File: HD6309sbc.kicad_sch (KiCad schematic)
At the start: 24 parts, among them J1 Conn_01x02_Male, J3 Conn_01x02_Male, U1 HD63C09, U11 74HC02, U12 74AHC1G08, U13 74HC21D, U14 74HC21D, U15 74HC21D, U4 UM61256FK, U6 28C256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

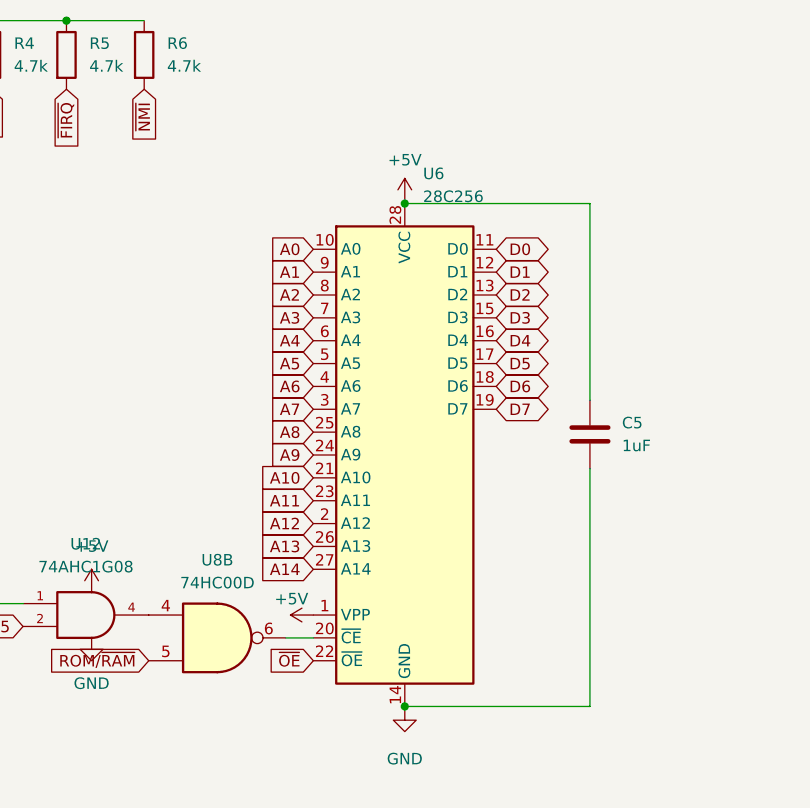
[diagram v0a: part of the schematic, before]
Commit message: fix rom footprint
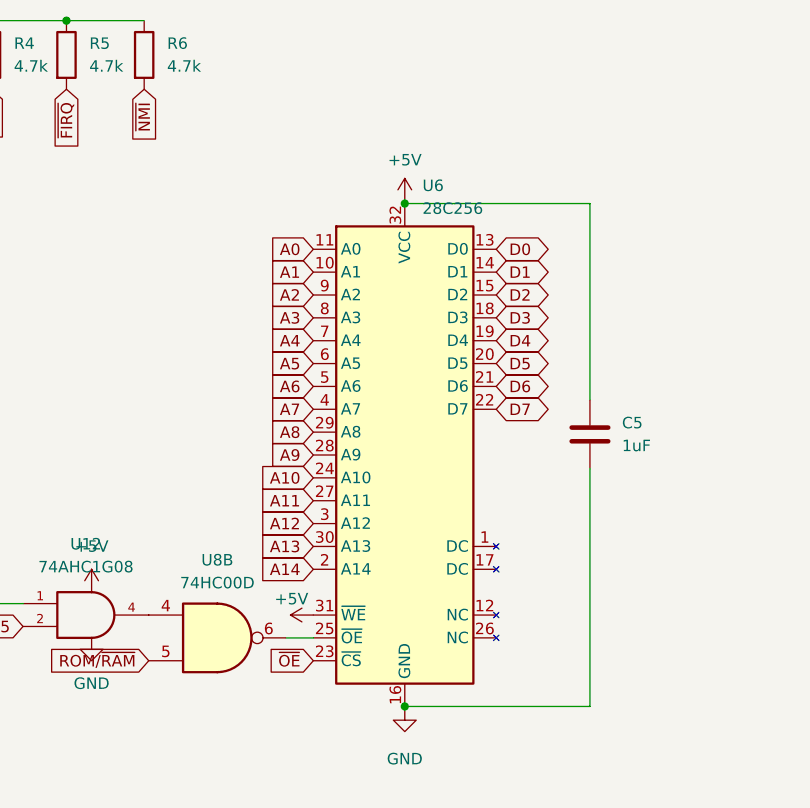
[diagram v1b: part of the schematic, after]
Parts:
- removed U6: 28C256, Package_LCC:PLCC-28_THT-Socket, symbol Memory_EPROM:27C256
- added U6: 28C256, Package_LCC:PLCC-32_THT-Socket, symbol 6309sbc:28C256plcc
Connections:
- net +5V: now also U6.31 (~{WE}), U6.32 (VCC)
- net A0: now also U6.11 (A0)
- net A1: now also U6.10 (A1)
- net A10: now also U6.24 (A10)
- net A11: now also U6.27 (A11)
- net A12: now also U6.3 (A12)
- net A13: now also U6.30 (A13)
- net A14: now also U6.2 (A14)
- net A2: now also U6.9 (A2)
- net A3: now also U6.8 (A3)
- net A4: now also U6.7 (A4)
- net A5: now also U6.6 (A5)
- net A6: now also U6.5 (A6)
- net A7: now also U6.4 (A7)
- net A8: now also U6.29 (A8)
- net A9: now also U6.28 (A9)
- net D0: now also U6.13 (D0)
- net D1: now also U6.14 (D1)
- net D2: now also U6.15 (D2)
- net D3: now also U6.18 (D3)
- net D4: now also U6.19 (D4)
- net D5: now also U6.20 (D5)
- net D6: now also U6.21 (D6)
- net D7: now also U6.22 (D7)
- net GND: now also U6.16 (GND)
- net ~{OE}: now also U6.23 (~{CS})
- net at U8.6: now also U6.25 (~{OE})
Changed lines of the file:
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@@
   (junction (at 35.306 25.654) (diameter 0) (color 0 0 0 0)
   )
+  (junction (at 42.926 25.654) (diameter 0) (color 0 0 0 0)
+  )
+  (junction (at 36.576 30.48) (diameter 0) (color 0 0 0 0)
+  )
+  (junction (at 38.1 191.262) (diameter 0) (color 0 0 0 0)
+  )
   (junction (at 147.574 132.08) (diameter 0) (color 0 0 0 0)
   )
-  (junction (at 42.926 25.654) (diameter 0) (color 0 0 0 0)
-  )
-  (junction (at 36.576 30.48) (diameter 0) (color 0 0 0 0)
-  )
-  (junction (at 38.1 191.262) (diameter 0) (color 0 0 0 0)
+  (junction (at 154.686 29.972) (diameter 0) (color 0 0 0 0)
+  )
+  (junction (at 93.218 111.76) (diameter 0) (color 0 0 0 0)
+  )
+  (junction (at 38.1 146.812) (diameter 0) (color 0 0 0 0)
   )
   (junction (at 147.574 187.96) (diameter 0) (color 0 0 0 0)
-  )
-  (junction (at 154.686 29.972) (diameter 0) (color 0 0 0 0)
-  )
-  (junction (at 93.218 111.76) (diameter 0) (color 0 0 0 0)
-  )
-  (junction (at 38.1 146.812) (diameter 0) (color 0 0 0 0)
   )
   (junction (at 101.6 111.76) (diameter 0) (color 0 0 0 0)
@@
         (path "/b6976bcd-dc73-4942-aa19-f7adbf9104c7"
           (reference "#PWR018") (unit 1)
+        )
+      )
+    )
+  )
+  (symbol (lib_id "6309sbc:28C256plcc") (at 147.574 160.02 0) (unit 1)
+    (in_bom yes) (on_board yes) (dnp no) (fields_autoplaced)
+    (property "Reference" "U6" (at 149.5299 130.0988 0)
+      (effects (font (size 1.27 1.27)) (justify left))
+    )
+    (property "Value" "28C256" (at 149.5299 132.6388 0)
+      (effects (font (size 1.27 1.27)) (justify left))
+    )
+    (property "Footprint" "Package_LCC:PLCC-32_THT-Socket" (at 147.574 160.02 0)
+      (effects (font (size 1.27 1.27)) hide)
+    )
+    (property "Datasheet" "http://ww1.microchip.com/downloads/en/DeviceDoc/doc0006.pdf" (at 147.574 160.02 0)
+      (effects (font (size 1.27 1.27)) hide)
+    )
+    (pin "1")
+    (pin "10")
+    (pin "11")
+    (pin "12")
+    (pin "13")
+    (pin "14")
+    (pin "15")
+    (pin "16")
+    (pin "17")
+    (pin "18")
+    (pin "19")
+    (pin "2")
+    (pin "20")
+    (pin "21")
+    (pin "22")
+    (pin "23")
+    (pin "24")
+    (pin "25")
+    (pin "26")
+    (pin "27")
+    (pin "28")
+    (pin "29")
+    (pin "3")
+    (pin "30")
+    (pin "31")
+    (pin "32")
+    (pin "4")
+    (pin "5")
+    (pin "6")
+    (pin "7")
+    (pin "8")
+    (pin "9")
+    (instances
+      (project "HD6309sbc"
+        (path "/b6976bcd-dc73-4942-aa19-f7adbf9104c7"
+          (reference "U6") (unit 1)
         )
       )
@@
         )
       )
-    )
-  )
-  (symbol (lib_id "Memory_EPROM:27C256") (at 147.574 160.02 0) (unit 1)
-    (in_bom yes) (on_board yes) (dnp no) (fields_autoplaced)
-    (property "Reference" "U6" (at 149.5934 128.778 0)
-      (effects (font (size 1.27 1.27)) (justify left))
-    )
-    (property "Value" "28C256" (at 149.5934 131.318 0)
-      (effects (font (size 1.27 1.27)) (justify left))
-    )
-    (property "Footprint" "Package_LCC:PLCC-28_THT-Socket" (at 147.574 160.02 0)
-      (effects (font (size 1.27 1.27)) hide)
-    )
-    (property "Datasheet" "http://ww1.microchip.com/downloads/en/DeviceDoc/doc0014.pdf" (at 147.574 160.02 0)
-      (effects (font (size 1.27 1.27)) hide)
-    )
-    (property "Note" "High 32k ROM" (at 147.574 160.02 0)
-      (effects (font (size 1.27 1.27)) hide)
-    )
-    (pin "1")
-    (pin "10")
-    (pin "11")
-    (pin "12")
-    (pin "13")
-    (pin "14")
-    (pin "15")
-    (pin "16")
-    (pin "17")
-    (pin "18")
-    (pin "19")
-    (pin "2")
-    (pin "20")
-    (pin "21")
-    (pin "22")
-    (pin "23")
-    (pin "24")
-    (pin "25")
-    (pin "26")
-    (pin "27")
-    (pin "28")
-    (pin "3")
-    (pin "4")
-    (pin "5")
-    (pin "6")
-    (pin "7")
-    (pin "8")
-    (pin "9")
-    (instances
-      (project "HD6309sbc"
-        (path "/b6976bcd-dc73-4942-aa19-f7adbf9104c7"
-          (reference "U6") (unit 1)
-        )
-      )

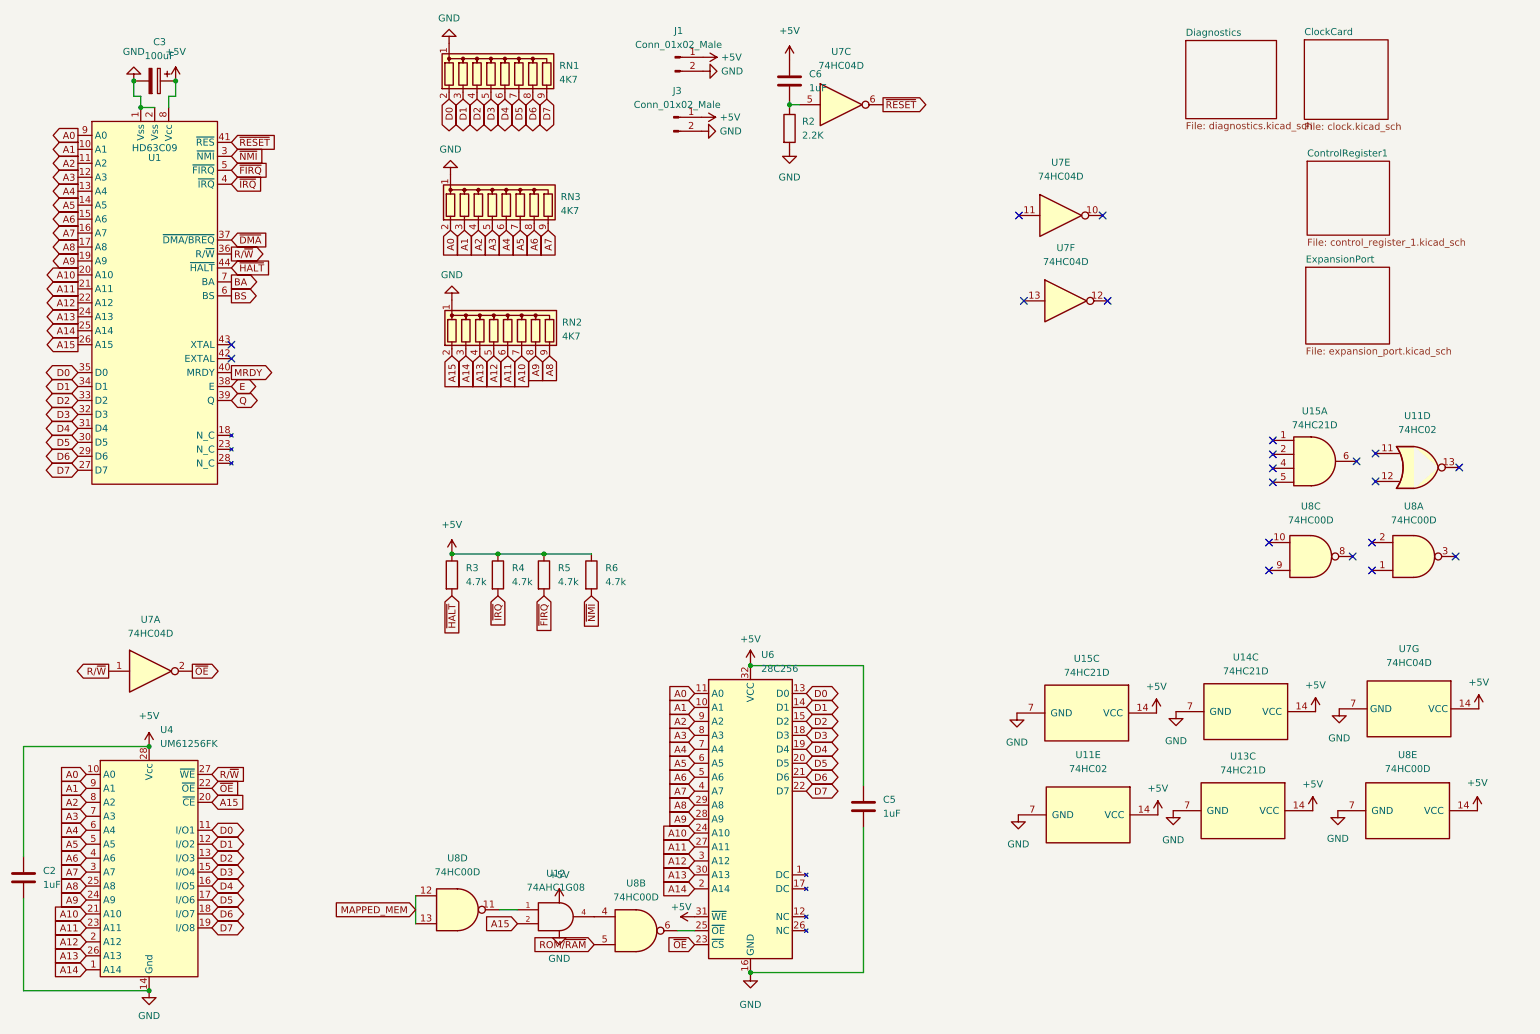
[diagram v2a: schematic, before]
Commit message: Refine reset circuit
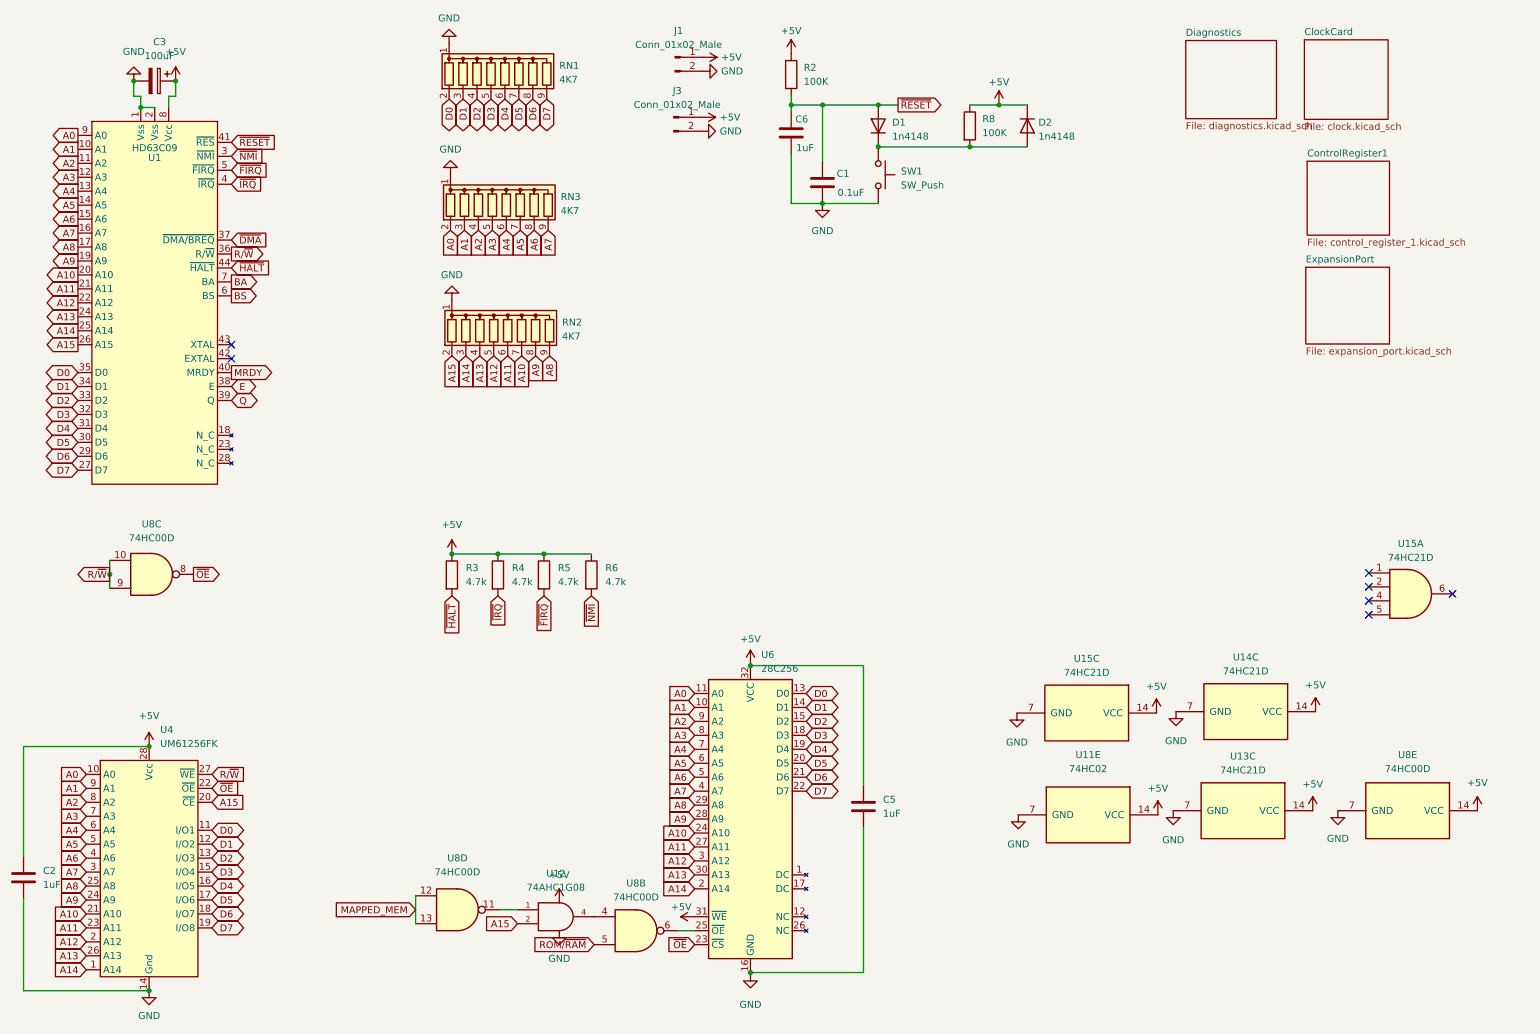
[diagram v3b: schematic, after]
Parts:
- removed unit 4 of U11
- removed U7: 74HC04D, Package_SO:SOIC-14_3.9x8.7mm_P1.27mm, symbol 74xx:74HC04
- removed unit 1 of U8
- added C1: 0.1uF, Capacitor_SMD:C_0805_2012Metric_Pad1.18x1.45mm_HandSolder, symbol Device:C
- added D1, D2: 1n4148, Diode_SMD:D_0805_2012Metric_Pad1.15x1.40mm_HandSolder, symbol Device:D
- added R8: 100K, Resistor_SMD:R_0805_2012Metric_Pad1.20x1.40mm_HandSolder, symbol Device:R
- added SW1: SW_Push, Button_Switch_SMD:SW_SPST_B3S-1000, symbol Switch:SW_Push
- R2: value 2.2K -> 100K
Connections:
- net +5V: now also R2.1, D2.1 (K), R8.1; no longer C6.1
- net GND: now also C6.2, C1.2, SW1.2; no longer R2.2
- net R/~{W}: now also U8.10, U8.9
- net ~{OE}: now also U8.8
- net ~{RESET}: now also C6.1, R2.2, C1.1, D1.2 (A)
- new net: D1.1 (K), D2.2 (A), R8.2, SW1.1
- no-connect marks 20 -> 7
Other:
- moved on the sheet: C6, R2, U15A, U8C

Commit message: convert to new format
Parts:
- removed C1: 0.1uF, Capacitor_SMD:C_0805_2012Metric_Pad1.18x1.45mm_HandSolder, symbol Device:C
- removed C2, C5, C6: 1uF, Capacitor_SMD:C_0805_2012Metric_Pad1.18x1.45mm_HandSolder, symbol Device:C
- removed D1, D2: 1n4148, Diode_SMD:D_0805_2012Metric_Pad1.15x1.40mm_HandSolder, symbol Device:D
- removed U11: 74HC02, Package_SO:SO-14_3.9x8.65mm_P1.27mm, symbol 74xx:74LS02
- removed U12: 74AHC1G08, Package_SO:TSOP-5_1.65x3.05mm_P0.95mm, symbol 74xGxx:74AHC1G08
- removed U13, U14, U15: 74HC21D, Package_SO:SOIC-14_3.9x8.7mm_P1.27mm, symbol 74xx:74LS21
- removed U4: UM61256FK, Package_DIP:DIP-28_W7.62mm, symbol 6309sbc:UM61256FK
- removed U6: 28C256, Package_LCC:PLCC-32_THT-Socket, symbol 6309sbc:28C256plcc
- removed U8: 74HC00D, Package_SO:SOIC-14_3.9x8.7mm_P1.27mm, symbol 74xx:74HC00
- added D1: RED, LED_SMD:LED_0805_2012Metric_Pad1.15x1.40mm_HandSolder, symbol Device:LED
- added D2: YELLOW, LED_SMD:LED_0805_2012Metric_Pad1.15x1.40mm_HandSolder, symbol Device:LED
- added D3: GREEN, LED_SMD:LED_0805_2012Metric_Pad1.15x1.40mm_HandSolder, symbol Device:LED
- added R9: 330R, Resistor_SMD:R_0805_2012Metric_Pad1.20x1.40mm_HandSolder, symbol Device:R
- added U2: DS1813, Package_TO_SOT_SMD:SOT-23-3, symbol 6309sbc:DS1813
- added U3: 74AHC1G14, Package_TO_SOT_SMD:SOT-353_SC-70-5_Handsoldering, symbol 74xGxx:74AHC1G14
- R2, R8: value 100K -> 330R
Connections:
- net +5V: now also D3.2 (A), U2.2 (VCC), U3.5 (VCC); no longer R2.1, R8.1
- net GND: now also R2.2, R8.2, R9.2, U2.3 (GND), U3.3 (GND)
- net ~{RESET}: now also SW1.1, D2.2 (A), U2.1 (~{RST}), U3.2; no longer R2.2
- net LIC: now reaches U1.42 (EXTAL)
- net TSC: now reaches U1.43 (XTAL)
- net MRDY renamed AVMA
- net ~{DMA} renamed BUSY
- new net: D3.1 (K), R9.1
- new net: D2.1 (K), R8.1
- new net: D1.1 (K), R2.1
- new net: D1.2 (A), U3.4
- no-connect marks 7 -> 0
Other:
- removed sheet ControlRegister1
- added sheet GPR1 (gpr1.kicad_sch)
- added sheet MemoryDecoder (decoder.kicad_sch)
- sheet ClockCard ports: added intD[0..7]; removed none
- sheet Diagnostics ports: added intD[0..7]; removed none
- sheet ExpansionPort ports: added A[0..15], D[0..7]; removed none
- title: (none) -> HD6309 Homebrew SBC
- moved on the sheet: C3, R2, R3, R4, R5, R6, R8, RN2, RN3, SW1, U1

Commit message: clean up before redesign
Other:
- sheet ClockCard ports: added intD0[0..7]; removed intD[0..7]
- sheet Diagnostics ports: added intD0[0..7], intD1[0..7]; removed intD[0..7]
- sheet GPR1 ports: added intD0[0..7], intD1[0..7]; removed intD[0..7]

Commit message: update readme
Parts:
- removed D1: RED, LED_SMD:LED_0805_2012Metric_Pad1.15x1.40mm_HandSolder, symbol Device:LED
- removed D2: YELLOW, LED_SMD:LED_0805_2012Metric_Pad1.15x1.40mm_HandSolder, symbol Device:LED
- removed D3: GREEN, LED_SMD:LED_0805_2012Metric_Pad1.15x1.40mm_HandSolder, symbol Device:LED
- removed J1, J3: Conn_01x02_Male, Connector_PinHeader_2.54mm:PinHeader_1x02_P2.54mm_Vertical, symbol Connector:Conn_01x02_Male
- removed R2, R9: 330R, Resistor_SMD:R_0805_2012Metric_Pad1.20x1.40mm_HandSolder, symbol Device:R
- removed RN1, RN2, RN3: 4K7, Resistor_THT:R_Array_SIP9, symbol Device:R_Network08
- removed SW1: SW_Push, Button_Switch_SMD:SW_SPST_B3S-1000, symbol Switch:SW_Push
- removed U2: DS1813, Package_TO_SOT_SMD:SOT-23-3, symbol 6309sbc:DS1813
- removed U3: 74AHC1G14, Package_TO_SOT_SMD:SOT-353_SC-70-5_Handsoldering, symbol 74xGxx:74AHC1G14
- added J2: Address Bus, Connector_PinHeader_2.54mm:PinHeader_1x16_P2.54mm_Vertical, symbol Connector_Generic:Conn_01x16
- added J4: Power, Connector_PinHeader_2.54mm:PinHeader_1x04_P2.54mm_Vertical, symbol Connector_Generic:Conn_01x04
- added J5: quadrature, Connector_PinSocket_2.54mm:PinSocket_1x04_P2.54mm_Vertical, symbol Connector_Generic:Conn_01x04
- added J6: Data Bus, Connector_PinHeader_2.54mm:PinHeader_1x08_P2.54mm_Vertical, symbol Connector_Generic:Conn_01x08
- added J7: CPU Control, Connector_PinHeader_2.54mm:PinHeader_1x08_P2.54mm_Vertical, symbol Connector_Generic:Conn_01x08
- added J8: Interrupts, Connector_PinHeader_2.54mm:PinHeader_1x04_P2.54mm_Vertical, symbol Connector_Generic:Conn_01x04
- added R7: 4.7k, Resistor_SMD:R_0805_2012Metric_Pad1.20x1.40mm_HandSolder, symbol Device:R
- R8: value 330R -> 4.7k
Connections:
- net +5V: now also J4.2 (Pin_2), J4.3 (Pin_3), R7.1
- net A0: now also J2.1 (Pin_1)
- net A1: now also J2.2 (Pin_2)
- net A10: now also J2.11 (Pin_11)
- net A11: now also J2.12 (Pin_12)
- net A12: now also J2.13 (Pin_13)
- net A13: now also J2.14 (Pin_14)
- net A14: now also J2.15 (Pin_15)
- net A15: now also J2.16 (Pin_16)
- net A2: now also J2.3 (Pin_3)
- net A3: now also J2.4 (Pin_4)
- net A4: now also J2.5 (Pin_5)
- net A5: now also J2.6 (Pin_6)
- net A6: now also J2.7 (Pin_7)
- net A7: now also J2.8 (Pin_8)
- net A8: now also J2.9 (Pin_9)
- net A9: now also J2.10 (Pin_10)
- net AVMA: now also J7.4 (Pin_4)
- net BA: now also J7.8 (Pin_8)
- net BS: now also J7.7 (Pin_7)
- net BUSY: now also J7.1 (Pin_1)
- net D0: now also J6.1 (Pin_1)
- net D1: now also J6.2 (Pin_2)
- net D2: now also J6.3 (Pin_3)
- net D3: now also J6.4 (Pin_4)
- net D4: now also J6.5 (Pin_5)
- net D5: now also J6.6 (Pin_6)
- net D6: now also J6.7 (Pin_7)
- net D7: now also J6.8 (Pin_8)
- net E: now also J5.1 (Pin_1)
- net GND: now also J4.1 (Pin_1), J4.4 (Pin_4)
- net LIC: now also J7.6 (Pin_6)
- net Q: now also J5.4 (Pin_4)
- net R/~{W}: now also J7.2 (Pin_2)
- net TSC: now also R8.1, J7.5 (Pin_5)
- net ~{FIRQ}: now also J8.2 (Pin_2)
- net ~{HALT}: now also J7.3 (Pin_3)
- net ~{IRQ}: now also J8.3 (Pin_3)
- net ~{NMI}: now also J8.4 (Pin_4)
- net ~{RESET}: now also J5.3 (Pin_3), J8.1 (Pin_1), R7.2
- no-connect marks 0 -> 1
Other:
- removed sheet ClockCard
- removed sheet Diagnostics
- removed sheet ExpansionPort
- removed sheet GPR1
- removed sheet MemoryDecoder
- moved on the sheet: R3, R4, R5, R6
